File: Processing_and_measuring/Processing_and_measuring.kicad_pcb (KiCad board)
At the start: 2 copper layers, 36 parts, among them J1 Conn_02x07_Counter_Clockwise, J2 Conn_01x02_Pin, J3 Conn_02x07_Counter_Clockwise, U1 TPL7407LAD, U2 CD74HC4067M, U3 AVR128DA48x-xPT, U4 TPL7407LAD, Y1 X_Crystal_16MHz_18pF

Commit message: Layout work and power
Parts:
- added REF**: MountingHole_3.2mm_M3, MountingHole:MountingHole_3.2mm_M3, F.Cu at (109.5, 93.5)
- added REF**: MountingHole_3.2mm_M3, MountingHole:MountingHole_3.2mm_M3, F.Cu at (194.0, 51.5)
- added REF**: MountingHole_3.2mm_M3, MountingHole:MountingHole_3.2mm_M3, F.Cu at (112.5, 52.5)
- added REF**: MountingHole_3.2mm_M3, MountingHole:MountingHole_3.2mm_M3, F.Cu at (194.5, 96.0)
- moved C14 121.2 mm to (151.7, 96.5)
- moved C13 109.4 mm to (138.2, 96.5)
- moved R9 86.3 mm to (129.7, 62.0)
- moved R10 86.2 mm to (129.7, 64.0)
- moved R11 86.2 mm to (129.7, 66.0)
- moved R12 86.1 mm to (129.7, 68.0)
- moved R13 86.0 mm to (129.7, 70.0)
- moved R14 86.0 mm to (129.7, 72.0)
- moved R15 85.8 mm to (129.7, 74.0)
- moved R16 85.8 mm to (129.7, 76.5)
- moved R18 84.9 mm to (133.0, 47.5)
- moved R17 78.6 mm to (127.0, 49.8), turned to 90 degrees
- moved R1 75.0 mm to (108.5, 78.0), turned to 180 degrees
- moved C4 73.7 mm to (110.0, 57.5)
- moved R2 73.2 mm to (108.5, 76.0), turned to 180 degrees
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
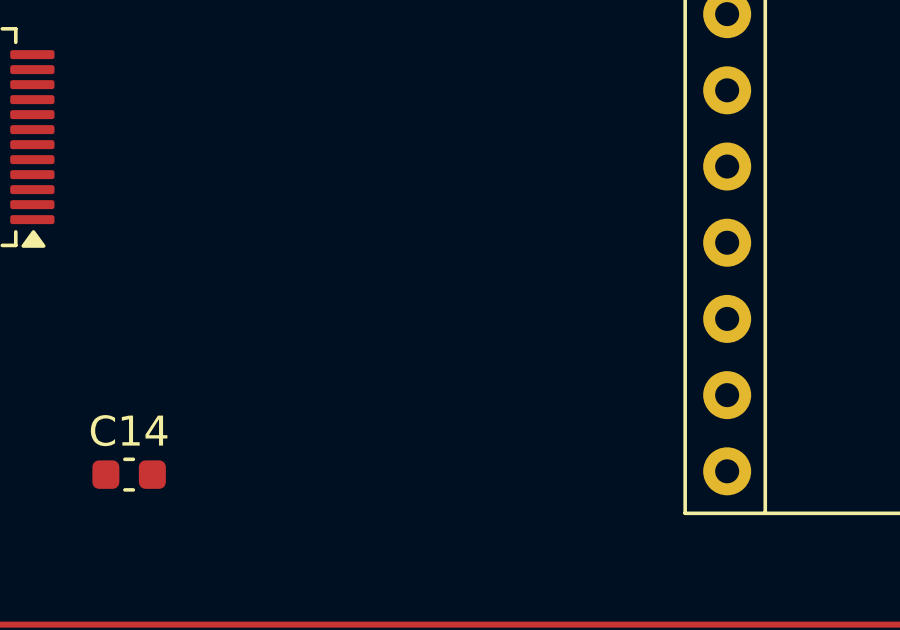
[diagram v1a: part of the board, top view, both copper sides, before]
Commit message: Addded footprint for buck converter
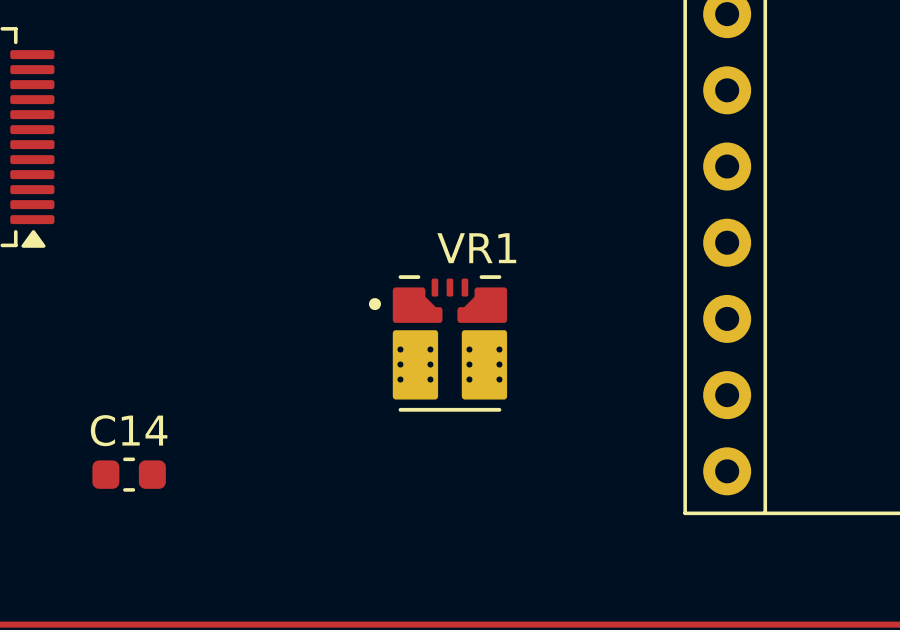
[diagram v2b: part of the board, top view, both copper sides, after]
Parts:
- added VR1: TPSM863253RDXR, TPSM863253RDXR:VREG_TPSM863253RDXR, F.Cu at (162.4, 92.2)

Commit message: More combining
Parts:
- removed J1: Conn_02x07_Counter_Clockwise, Connector_PinHeader_1.00mm:PinHeader_2x07_P1.00mm_Horizontal
- added J5: Conn_02x07_Counter_Clockwise, Connector_PinHeader_1.00mm:PinHeader_2x07_P1.00mm_Horizontal, F.Cu at (145.6, 58.2)
- moved VR1 24.5 mm to (174.2, 70.7), turned to -90 degrees
- moved A1 15.9 mm to (187.5, 77.5), turned to -90 degrees
- moved C14 3.79 mm to (148.5, 94.5), turned to -90 degrees
- moved C13 2.67 mm to (140.0, 94.5), turned to 90 degrees
- moved Y1 1.80 mm to (144.0, 94.5), turned to 180 degrees
- moved U1 0.99 mm to (143.0, 67.4)
- moved U4 0.30 mm to (156.1, 67.2)
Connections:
- A1 pad 8: unconnected-(A1-VMOT-Pad8) -> Power
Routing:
- net Power: track 0.00 -> 62.2 mm
- net Net-(J5-Pin_8): track 0.00 -> 16.4 mm
- net Net-(J5-Pin_6): track 0.00 -> 14.9 mm
- net Net-(J5-Pin_10): track 0.00 -> 14.5 mm
- net Net-(J5-Pin_4): track 0.00 -> 12.4 mm
- net Net-(J5-Pin_12): track 0.00 -> 12.0 mm
- net Net-(J5-Pin_2): track 0.00 -> 9.90 mm
- net Net-(U3-PA0): track 0.00 -> 9.89 mm
- net Net-(J5-Pin_14): track 0.00 -> 9.51 mm
- net GND: track 0.00 -> 8.93 mm, vias 0 -> 3
- net Net-(U2-I15): track 0.00 -> 8.18 mm
- net Net-(J5-Pin_1): track 0.00 -> 8.03 mm
- net Net-(J5-Pin_3): track 0.00 -> 7.91 mm
- net Net-(U3-PA1): track 0.00 -> 7.87 mm
- net Net-(J5-Pin_5): track 0.00 -> 7.80 mm
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- added copper zone on B.Cu, net GND
- added copper zone on F.Cu, net Power

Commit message: more changes to layout
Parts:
- removed J5: Conn_02x07_Counter_Clockwise, Connector_PinHeader_1.00mm:PinHeader_2x07_P1.00mm_Horizontal
- added J1: Conn_02x07_Counter_Clockwise, Connector_PinHeader_1.00mm:PinHeader_2x07_P1.00mm_Horizontal, F.Cu at (145.7, 57.8)
- added J4: Conn_01x04_Pin, Connector_PinHeader_1.00mm:PinHeader_1x04_P1.00mm_Horizontal, F.Cu at (164.0, 40.9)
- L1: footprint Capacitor_SMD:C_0603_1608Metric -> Inductor_SMD:L_0603_1608Metric
- R1, R10, R11, R12, R13, R14, R15, R16, R17, R18, R19, R2, R20, R3, R4, R5, R6, R7, R8, R9: footprint Capacitor_SMD:C_0603_1608Metric -> Resistor_SMD:R_0603_1608Metric
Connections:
- A1 pad 8: Power -> unconnected-(A1-VMOT-Pad8)
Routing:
- net /DIR: track 0.00 -> 43.1 mm
- net /STEP: track 0.00 -> 43.1 mm, vias 0 -> 1
- net /DOUT2: track 0.00 -> 36.2 mm
- net /DOUT1: track 0.00 -> 34.9 mm
- net /DOUT4: track 0.00 -> 29.2 mm, vias 0 -> 2
- net /DOUT3: track 0.00 -> 26.6 mm
- net /motor4: track 0.00 -> 21.9 mm
- net Net-(J1-Pin_4): track 12.4 -> 13.2 mm
- net Net-(J1-Pin_12): track 12.0 -> 12.7 mm
- net Net-(J1-Pin_8): track 16.4 -> 17.1 mm

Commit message: Lots of progress made on assembly
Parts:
- added C5: 22u, Capacitor_SMD:C_0603_1608Metric, F.Cu at (178.7, 70.0)
- added J5: Conn_01x02_Pin, Connector_PinHeader_1.00mm:PinHeader_1x02_P1.00mm_Horizontal, F.Cu at (181.5, 42.3)
- added J6: Conn_01x02_Pin, Connector_PinHeader_1.00mm:PinHeader_1x02_P1.00mm_Horizontal, F.Cu at (195.4, 88.7)
- added kibuzzard-6920BB03: G***, kibuzzard-6920BB03, F.Cu at (142.9, 54.2)
- added kibuzzard-6920BB24: G***, kibuzzard-6920BB24, F.Cu at (164.6, 55.0)
- added kibuzzard-6920BBD9: G***, kibuzzard-6920BBD9, F.Cu at (123.2, 98.9)
- added kibuzzard-6920BC10: G***, kibuzzard-6920BC10, F.Cu at (123.5, 95.9)
- C13, C14: value C_30pF -> C_33pF
- C3: value 44u -> 22u
- moved R19 75.9 mm to (173.6, 71.0), turned to 180 degrees
- moved C4 67.3 mm to (176.5, 67.8)
- moved C1 64.7 mm to (138.3, 94.3), turned to -90 degrees
- moved R20 58.6 mm to (173.4, 68.5)
- moved C2 54.2 mm to (136.5, 83.2), turned to 90 degrees
- moved R17 49.5 mm to (173.3, 67.2), turned to 180 degrees
- moved J4 48.9 mm to (195.0, 78.7)
- moved R18 48.7 mm to (176.5, 69.4), turned to 180 degrees
- moved L1 39.3 mm to (138.8, 91.8)
- moved C3 33.1 mm to (111.2, 80.7)
- moved VR1 7.00 mm to (167.9, 67.5)
- moved REF** 3.07 mm to (109.5, 53.1)
- moved REF** 2.35 mm to (109.5, 95.8)
- moved REF** 1.72 mm to (194.5, 53.1)
- moved REF** 0.16 mm to (194.4, 95.8)
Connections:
- A1 pad 3: unconnected-(A1-1B-Pad3) -> /3
- A1 pad 4: unconnected-(A1-1A-Pad4) -> /4
- A1 pad 5: unconnected-(A1-2A-Pad5) -> /5
- A1 pad 6: unconnected-(A1-2B-Pad6) -> /6
- A1 pad 8: unconnected-(A1-VMOT-Pad8) -> Power
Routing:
- net Power: track 62.2 -> 134.4 mm
- net +5V: track 0.00 -> 65.5 mm
- net /RXD: track 0.00 -> 52.3 mm, vias 0 -> 2
- net /TXD: track 0.00 -> 50.2 mm, vias 0 -> 2
- net /Read: track 0.00 -> 40.5 mm, vias 0 -> 2
- net /motor7: track 0.00 -> 27.4 mm, vias 0 -> 2
- net /motor6: track 0.00 -> 25.0 mm, vias 0 -> 2
- net /6: track 0.00 -> 24.8 mm, vias 0 -> 2
- net /motor5: track 0.00 -> 23.2 mm, vias 0 -> 2
- net /motor8: track 0.00 -> 22.3 mm
- net GND: track 8.93 -> 30.8 mm, vias 3 -> 10
- net /motor9: track 0.00 -> 21.2 mm
- net /motor10: track 0.00 -> 20.2 mm
- net /5: track 0.00 -> 20.1 mm
- net /motor11: track 0.00 -> 19.1 mm
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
